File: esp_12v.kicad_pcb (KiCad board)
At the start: 2 copper layers, 84.1 x 25 mm, 18 parts, among them J1 12V Input, J2 12V for Load, J3 UART, Q1 IRLZ44N, SW1 SW_Push, U1 ESP-01v090, U2 R-78E3.3-0.5, U3 DHT11

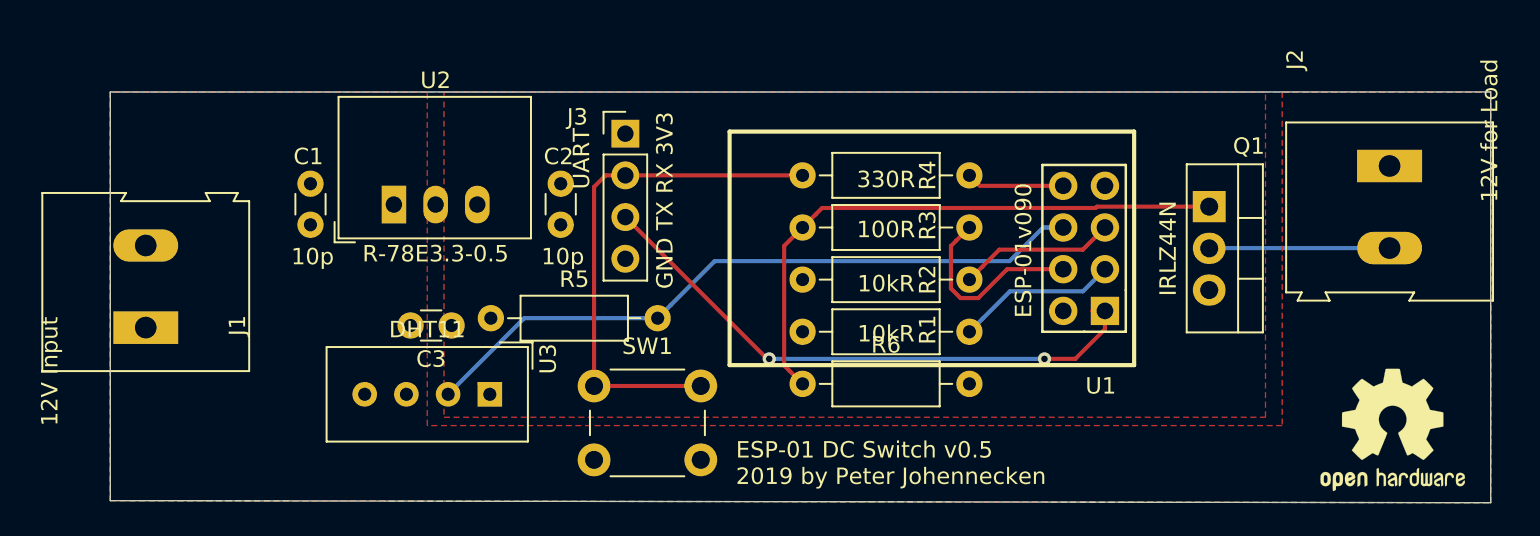
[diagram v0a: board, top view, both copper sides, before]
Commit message: bumped to Version 0.6
* changed dc jacks to terminalblocks
* added decoupling cap for the thermal sensor
* added 10kR between Gate and GND at the mosfet
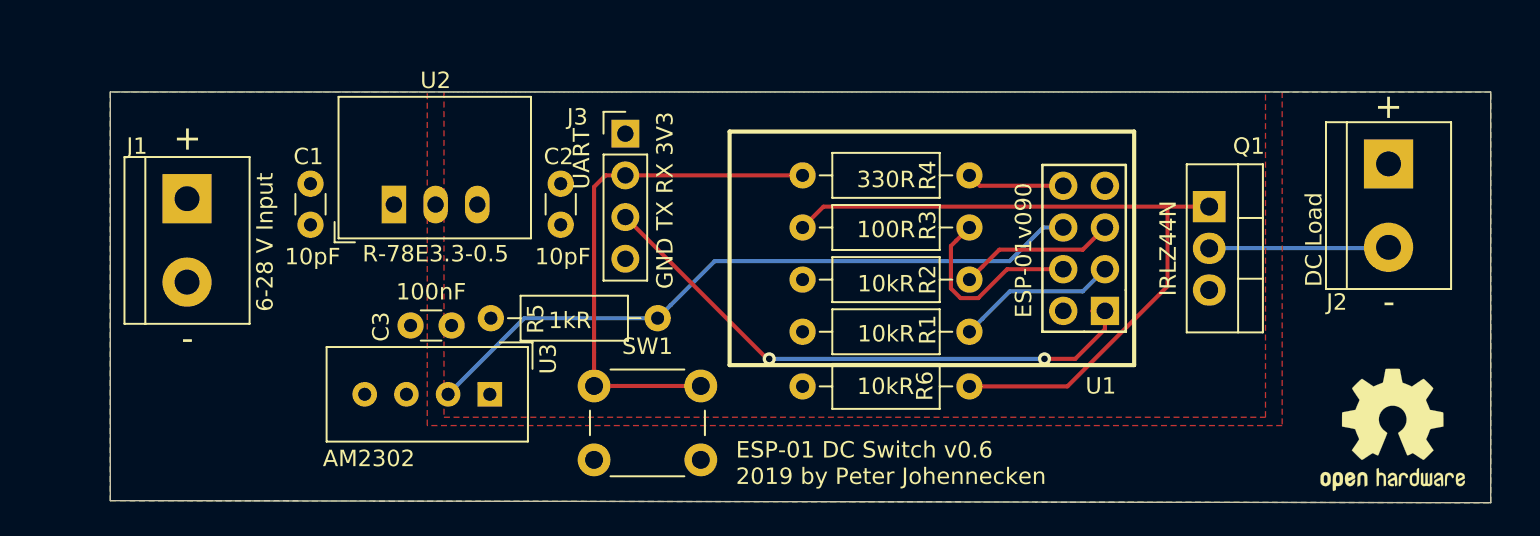
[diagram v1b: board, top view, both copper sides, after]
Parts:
- C1, C2: value 10p -> 10pF
- J1: value 12V Input -> 6-28 V Input; footprint TerminalBlock:TerminalBlock_Altech_AK300-2_P5.00mm -> TerminalBlock:TerminalBlock_bornier-2_P5.08mm
- J2: value 12V for Load -> DC Load; footprint TerminalBlock:TerminalBlock_Altech_AK300-2_P5.00mm -> TerminalBlock:TerminalBlock_bornier-2_P5.08mm
- U3: value DHT11 -> AM2302
- moved R6 10.2 mm to (78.7, 30.6), turned to 180 degrees
- moved J1 8.24 mm to (31.1, 19.2), turned to 270 degrees
- moved J2 0.14 mm to (104.3, 17.1)
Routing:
- net Net-(Q1-Pad1): track 35.7 -> 44.7 mm
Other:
- board text added: "+"
- board text added: "-"
- board text added: "ESP-01 DC Switch v0.6 2019 by Peter Johennecken"
- board text removed: "ESP-01 DC Switch v0.5 2019 by Peter Johennecken"
